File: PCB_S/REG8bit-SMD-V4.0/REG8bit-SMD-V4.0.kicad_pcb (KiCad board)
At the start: 4 copper layers, 118 parts, among them J2 Conn_01x21_Pin, Q1 2N7002, Q10 2N7002, Q11 2N7002, Q12 2N7002, Q13 2N7002, Q14 2N7002, Q15 2N7002, Q17 2N7002, Q19 2N7002, Q2 2N7002, Q20 2N7002, Q21 2N7002, Q22 2N7002, Q23 2N7002, Q24 2N7002, Q25 2N7002, Q27 2N7002, Q29 2N7002, Q3 2N7002, Q30 2N7002, Q31 2N7002, Q32 2N7002, Q33 2N7002, Q34 2N7002, Q35 2N7002, Q37 2N7002, Q39 2N7002, Q4 2N7002, Q40 2N7002, Q41 2N7002, Q42 2N7002, Q43 2N7002, Q44 2N7002, Q45 2N7002, Q47 2N7002, Q49 2N7002, Q5 2N7002, Q50 2N7002, Q51 2N7002, Q52 2N7002, Q53 2N7002, Q54 2N7002, Q55 2N7002, Q57 2N7002, Q59 2N7002, Q6 2N7002, Q60 2N7002, Q61 2N7002, Q62 2N7002, Q63 2N7002, Q64 2N7002, Q65 2N7002, Q67 2N7002, Q69 2N7002, Q70 2N7002, Q71 2N7002, Q72 2N7002, Q73 2N7002, Q74 2N7002, Q75 2N7002, Q77 2N7002, Q79 2N7002, Q80 2N7002, Q81 2N7002, Q82 2N7002, Q83 2N7002, Q84 2N7002, Q85 2N7002, Q86 2N7002, Q87 2N7002, Q88 2N7002, Q89 2N7002, Q9 2N7002

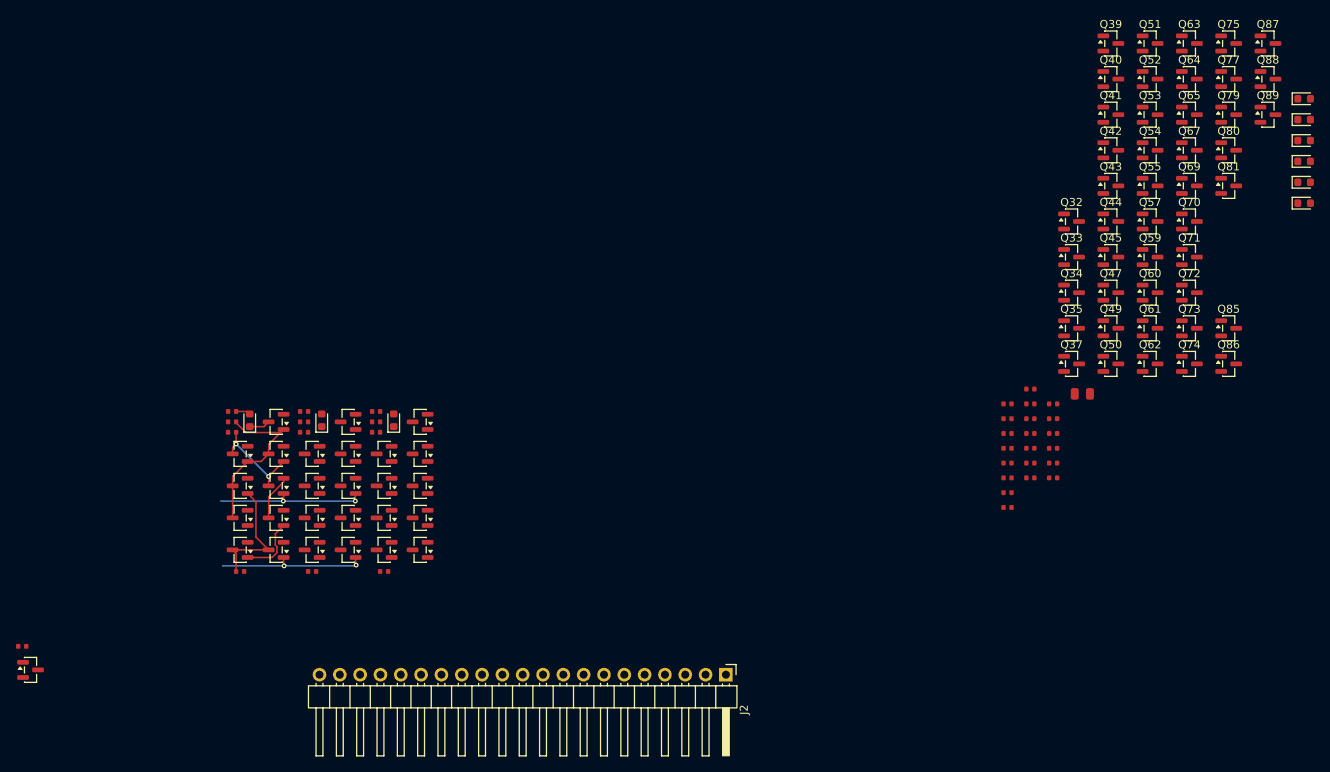
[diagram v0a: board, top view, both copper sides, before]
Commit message: New Register half done
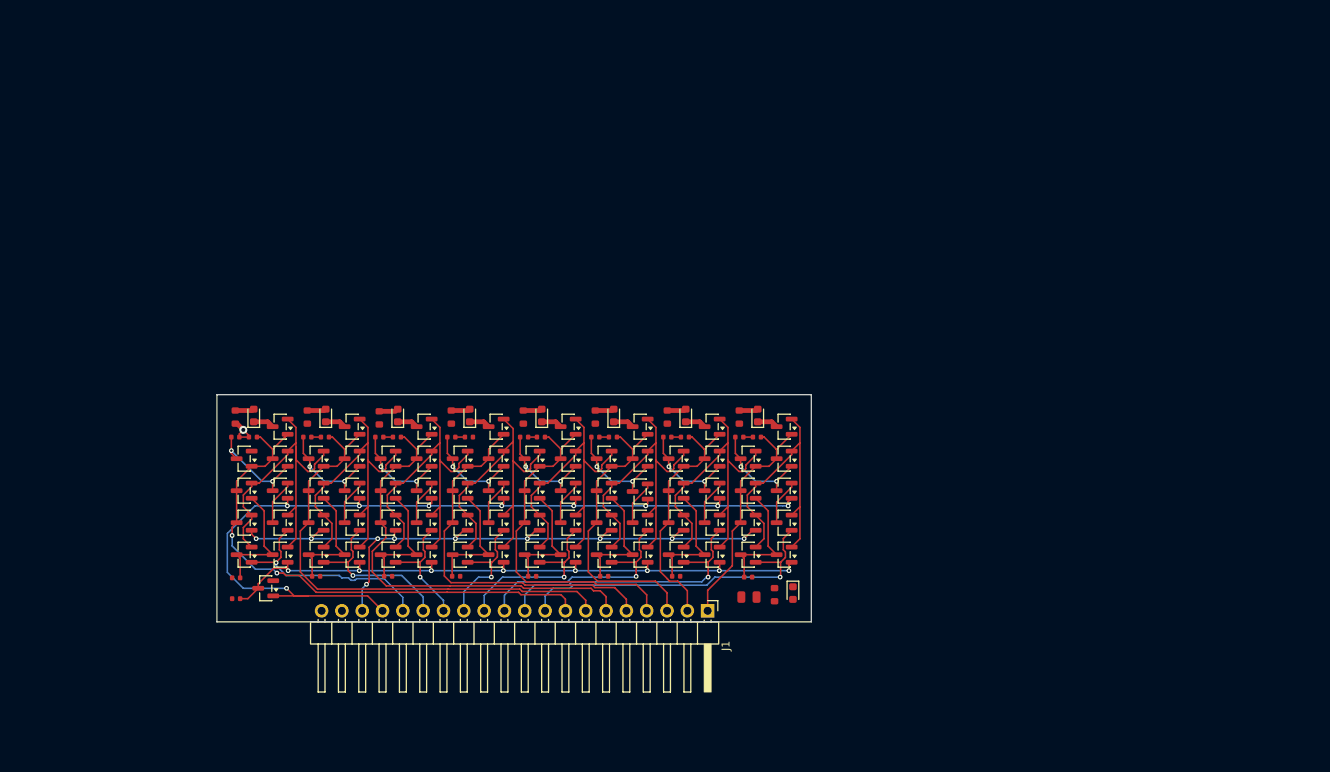
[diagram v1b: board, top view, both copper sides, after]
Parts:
- removed J2: Conn_01x21_Pin, Connector_PinHeader_2.54mm:PinHeader_1x21_P2.54mm_Horizontal
- removed R42, R43, R44, R45, R46, R47, R48, R49, R50: 470Ω, PCM_JLCPCB:R_0402
- added J1: Conn_01x20_Pin, Connector_PinHeader_2.54mm:PinHeader_1x20_P2.54mm_Horizontal, F.Cu at (108.4, 151.0)
- added R11: 470Ω, PCM_JLCPCB:R_0603, F.Cu at (67.4, 126.9)
- added R13: 470Ω, PCM_JLCPCB:R_0603, F.Cu at (76.4, 126.8)
- added R16: 470Ω, PCM_JLCPCB:R_0603, F.Cu at (85.4, 126.8)
- added R18: 470Ω, PCM_JLCPCB:R_0603, F.Cu at (94.4, 126.8)
- added R21: 470Ω, PCM_JLCPCB:R_0603, F.Cu at (103.4, 126.8)
- added R23: 470Ω, PCM_JLCPCB:R_0603, F.Cu at (112.4, 126.8)
- added R3: 470Ω, PCM_JLCPCB:R_0603, F.Cu at (116.8, 149.0)
- added R6: 470Ω, PCM_JLCPCB:R_0603, F.Cu at (49.4, 126.8)
- added R8: 470Ω, PCM_JLCPCB:R_0603, F.Cu at (58.4, 126.8)
- R1, R10, R12, R14, R15, R17, R19, R2, R20, R22, R24, R25, R27, R29, R30, R32, R34, R35, R37, R39, R4, R40, R5, R7, R9: value 20kΩ -> 10kΩ
- moved D4 111.6 mm to (78.7, 126.6), turned to 90 degrees
- moved D5 102.2 mm to (87.7, 126.6), turned to 90 degrees
- moved Q51 94.2 mm to (91.0, 140.0), turned to 180 degrees
- moved D6 92.9 mm to (96.7, 126.6), turned to 90 degrees
- moved Q39 92.7 mm to (82.0, 132.0), turned to 180 degrees
- moved Q40 92.5 mm to (82.0, 136.0), turned to 180 degrees
- moved Q85 92.4 mm to (82.0, 128.0), turned to 180 degrees
- moved Q41 92.2 mm to (82.0, 140.0), turned to 180 degrees
- moved Q87 91.9 mm to (100.0, 128.0), turned to 180 degrees
- moved Q52 90.5 mm to (95.5, 144.0), turned to 180 degrees
- moved Q42 88.2 mm to (86.5, 144.0), turned to 180 degrees
- moved Q63 87.4 mm to (109.0, 144.0), turned to 180 degrees
- moved Q32 87.0 mm to (77.5, 144.0), turned to 180 degrees
- moved Q75 84.8 mm to (113.5, 140.0), turned to 180 degrees
- moved Q53 84.2 mm to (100.0, 144.0), turned to 180 degrees
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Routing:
- net Earth: track 0.00 -> 329.3 mm
- net /R: track 18.7 -> 110.4 mm, vias 2 -> 9
- net /RST: track 0.00 -> 84.7 mm, vias 0 -> 10
- net Net-(J1-Pin_7): track 0.00 -> 62.3 mm
- net Net-(Q1-D): track 18.8 -> 79.4 mm, vias 2 -> 8
- net Net-(J1-Pin_6): track 0.00 -> 56.7 mm
- net Net-(J1-Pin_5): track 0.00 -> 47.2 mm
- net Net-(J1-Pin_8): track 21.4 -> 66.8 mm, vias 0 -> 2
- net Net-(J1-Pin_4): track 0.00 -> 43.3 mm
- net Net-(J1-Pin_9): track 0.00 -> 42.0 mm, vias 0 -> 1
- net Net-(J1-Pin_3): track 0.00 -> 37.0 mm
- net Net-(J1-Pin_10): track 0.00 -> 35.5 mm, vias 0 -> 1
- net Net-(J1-Pin_2): track 0.00 -> 30.7 mm
- net Net-(J1-Pin_1): track 0.00 -> 30.0 mm
- net Net-(J1-Pin_11): track 0.00 -> 29.0 mm, vias 0 -> 1
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- added copper zone on In2.Cu, net Earth
- added copper zone on In1.Cu, net VCC
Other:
- board outline added: 74.3 x 28.4 mm

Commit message: PCB : REG8bit v4 done
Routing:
- net VCC: track 13.1 -> 60.5 mm, vias 1 -> 16
- net Earth: track 329.3 -> 350.8 mm, vias 0 -> 12
- net Net-(J1-Pin_5): track 47.2 -> 49.8 mm
- net Net-(D9-Pad2): track 0.00 -> 2.40 mm
- net Net-(Q1-D): track 79.4 -> 80.1 mm
- net Net-(J1-Pin_11): track 29.0 -> 29.6 mm
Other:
- board size 74.3 x 28.4 mm -> 73.7 x 28.4 mm
- board text added: "+"
- board text added: "-"
- board text added: "0"
- board text added: "0 1 2 3 4 5 6 7"
- board text added: "1"
- board text added: "2"
- board text added: "3"
- board text added: "4"
- board text added: "5"
- board text added: "6"
- board text added: "7"
- board text added: "7 6 5 4 3 2 1 0"
- board text added: "MEM"
- board text added: "NAND"
- board text added: "NOR"
- board text added: "R"
- board text added: "Reg V4"
- board text added: "SJ"
- board text added: "data in"
- board text added: "data out"
- board text added: "rst"
- board text added: "| data in |"
- board text added: "| data out |"

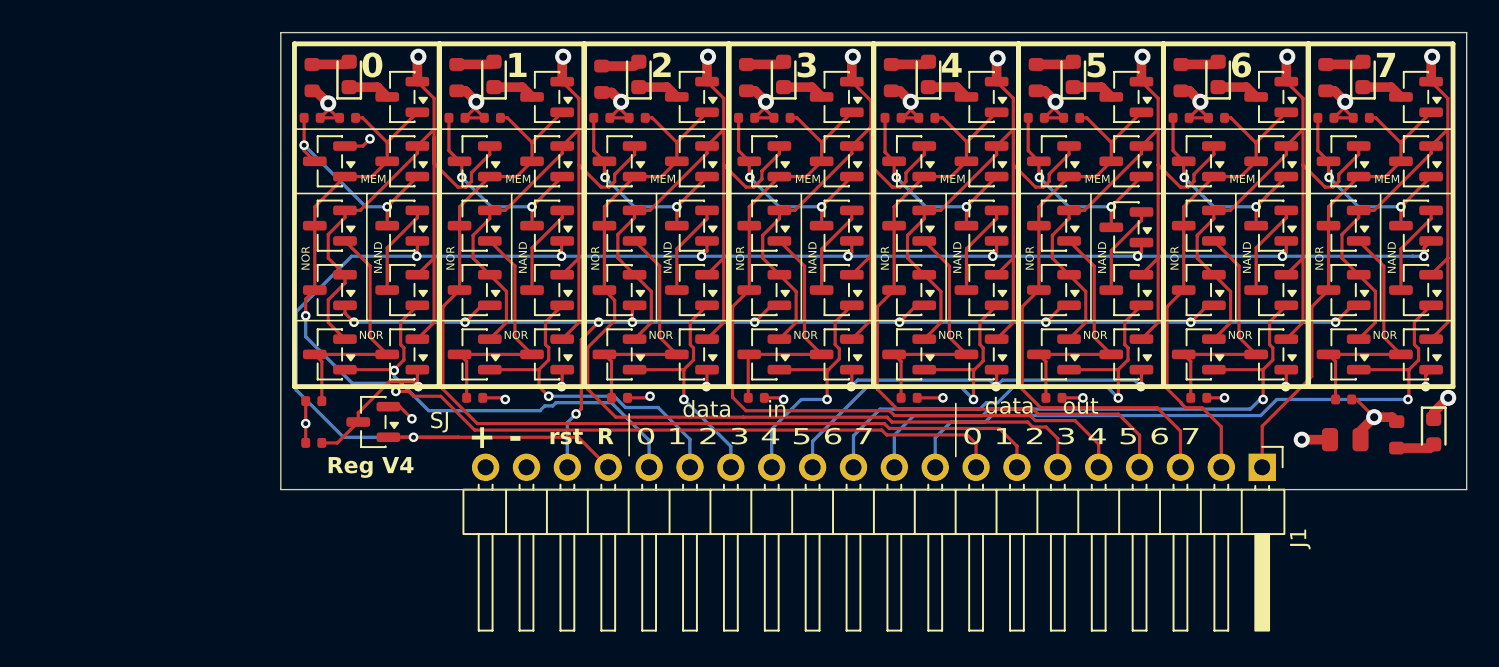
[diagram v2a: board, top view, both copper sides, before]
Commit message: sim
Tried the spice sim : the sim did not work at all
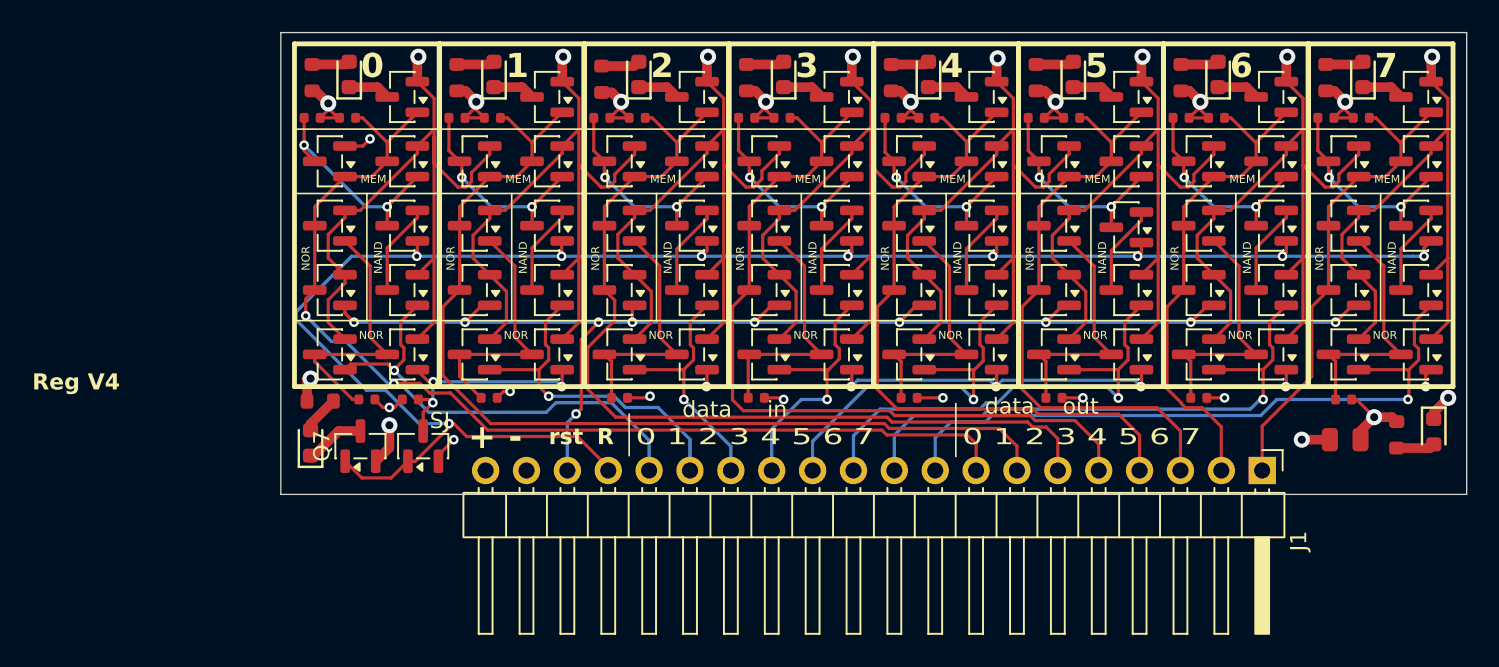
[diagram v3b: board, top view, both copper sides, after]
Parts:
- added D10: Red, PCM_JLCPCB:D_0603, F.Cu at (49.3, 149.5)
- added Q7: 2N7002, Package_TO_SOT_SMD:SOT-23, F.Cu at (52.4, 149.7)
- added R26: 2.2kΩ, PCM_JLCPCB:R_0603, F.Cu at (49.9, 146.9)
- R11, R13, R16, R18, R21, R23, R3, R6, R8: value 470Ω -> 2.2kΩ
- moved R1 6.58 mm to (55.5, 146.8)
- moved Q1 3.44 mm to (56.3, 149.7), turned to 90 degrees
- moved R2 3.30 mm to (52.8, 146.8), turned to 180 degrees
- moved R7 0.90 mm to (60.4, 146.7)
- moved J1 0.20 mm to (108.4, 151.2)
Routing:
- net Net-(Q1-D): track 80.1 -> 75.7 mm, vias 8 -> 9
- net Net-(Q7-D): track 0.00 -> 3.73 mm
- net Net-(D10-Pad2): track 0.00 -> 2.40 mm
- net VCC: track 60.5 -> 58.7 mm, vias 16 -> 17
- net /R: track 110.4 -> 112.1 mm
- net Net-(Q2-D): track 15.7 -> 16.8 mm
- net Earth: track 350.8 -> 351.7 mm, vias 12 -> 13
- net Net-(J1-Pin_16): track 27.8 -> 28.5 mm
- net Net-(J1-Pin_9): track 42.0 -> 42.6 mm
- net Net-(J1-Pin_8): track 66.8 -> 66.3 mm
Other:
- board size 73.7 x 28.4 mm -> 73.7 x 28.7 mm
